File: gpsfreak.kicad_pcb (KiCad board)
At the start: 4 copper layers, 79.8 x 47.2 mm, 177 parts, among them J13 Boot, J2 SMA, J3 SMA, J4 SMA, J5 U.Fl, J6 SMA, J7 USB_C_Receptacle_16P, J8 Conn_01x06, J9 Skedd, SW1 SW_Push, T2 MABA-010247-2R1250, U1 MAX-M10S, U2 LMK05318BRGZR, U3 TG5032CGN, U31 TLV3601DCKR, U4 STM32H503KBUx, U41 TS5A63157DBV, U5 TPSM82822SILR, U6 TPSM82822SILR, U61 TMP117xxDRV, U7 TPS7A8801RTJR, U71 USBLC6-2SC6, U8 LCMXO2-256HC-4SG32C

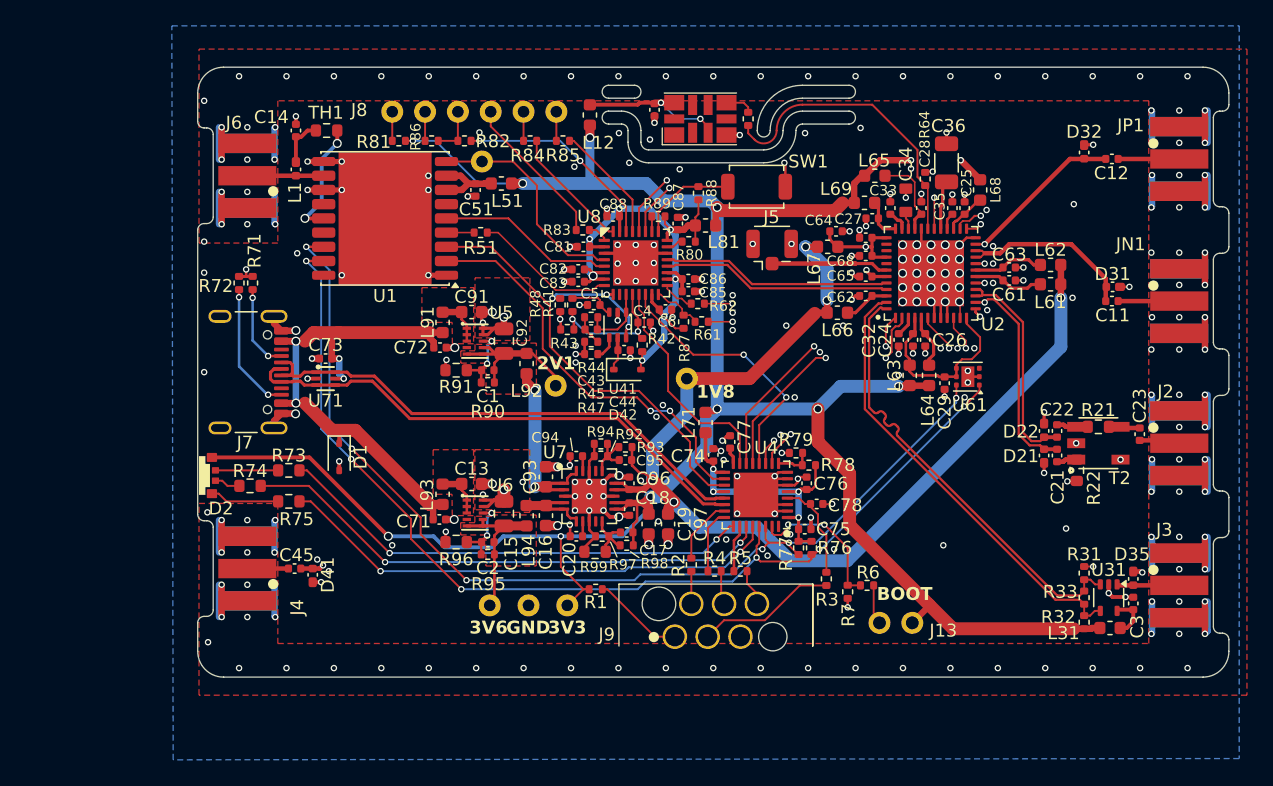
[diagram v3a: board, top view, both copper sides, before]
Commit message: Pull-up on safe-boot.  Juggle things a bit.
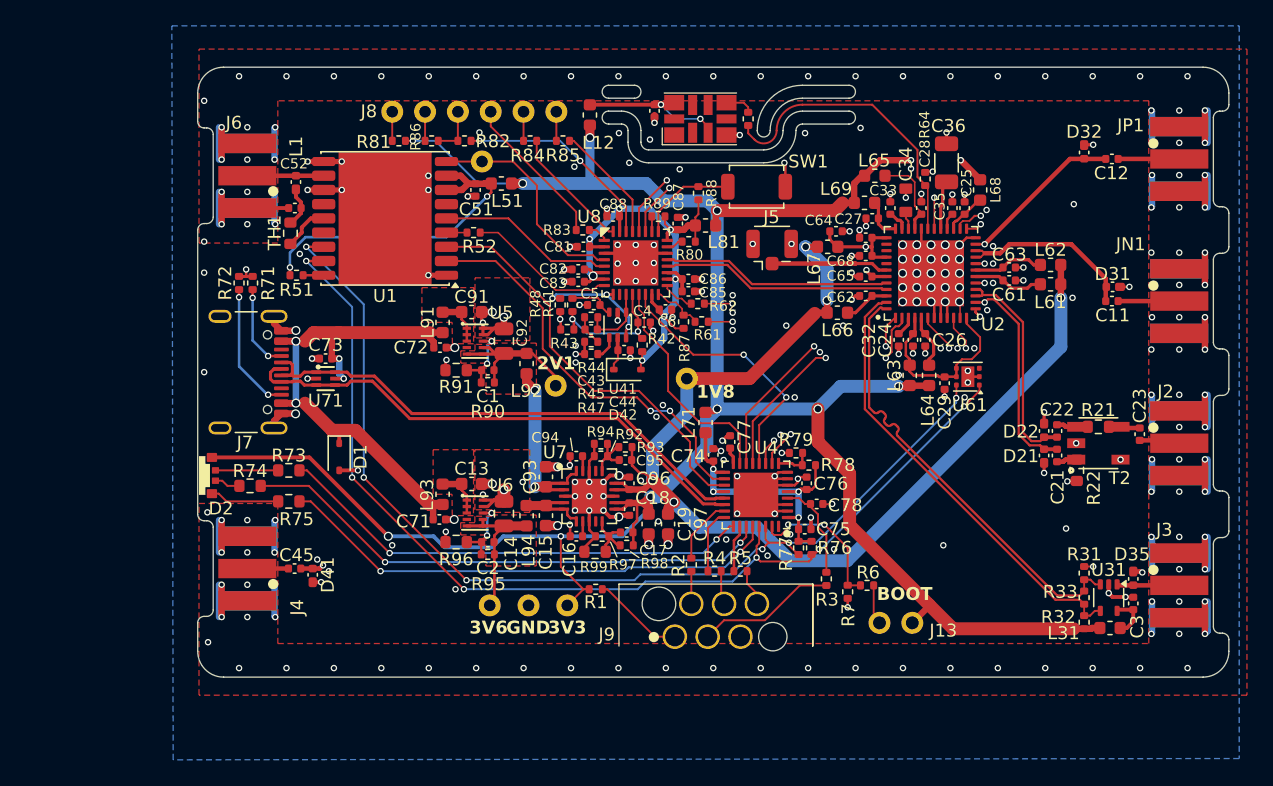
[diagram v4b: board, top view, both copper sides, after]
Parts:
- added R51: 5k1, Resistor_SMD:R_0402_1005Metric, F.Cu at (117.8, 92.5)
- moved TH1 8.43 mm to (117.3, 89.2), turned to -90 degrees
- moved C52 6.00 mm to (117.6, 87.3), turned to 180 degrees
- moved L1 0.97 mm to (117.7, 85.3), turned to -90 degrees
- moved R52 0.55 mm to (131.4, 89.2)
- moved C31 0.08 mm to (145.4, 79.8)
- renumbered C15 to C14, C16 to C15, C20 to C16, C14 to C52, R51 to R52
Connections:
- U1 pad 18: unconnected-(U1-~{SAFEBOOT}-Pad18) -> Net-(U1-~{SAFEBOOT})
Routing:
- net /GPS/VGPS: track 5.63 -> 25.6 mm, vias 0 -> 2
- net /GPS/VCC_RF: track 9.29 -> 3.63 mm, vias 2 -> 0
- net GND: track 206.9 -> 210.2 mm, vias 307 -> 306
- net Net-(U1-~{SAFEBOOT}): track 0.00 -> 1.59 mm
- net Net-(C52-Pad1): track 3.71 -> 3.13 mm
- net Net-(U1-TIMEPULSE): track 2.14 -> 1.59 mm
- net GPSCLK: track 11.0 -> 11.6 mm

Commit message: Tidy up.
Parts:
- added R11: 5k1, Resistor_SMD:R_0402_1005Metric, F.Cu at (146.8, 86.3)
- D42: value 1N5819WS -> RB751S-40; footprint Diode_SMD:D_SOD-323 -> Diode_SMD:D_SOD-523
- U8: value LCMXO2-256HC-4SG32C -> LCMXO2-640HC-4SG48C; footprint Parts:QFN-32-1EP_5x5mm_P0.5mm_EP3.5x3.5mm -> Parts:QFN-48-1EP_7x7mm_P0.5mm_EP5.45x5.45mm
- moved TP4 7.64 mm to (135.6, 93.8)
- moved R42 6.19 mm to (138.3, 97.2), turned to -90 degrees
- moved R87 3.56 mm to (146.2, 99.3), turned to 0 degrees
- moved C83 2.66 mm to (139.3, 95.7)
- moved R41 2.41 mm to (139.3, 97.2)
- moved C85 2.36 mm to (148.2, 96.1), turned to -90 degrees
- moved R45 2.31 mm to (140.8, 100.0), turned to 90 degrees
- moved C87 2.09 mm to (145.8, 87.0)
- moved C84 2.03 mm to (145.8, 97.1), turned to -90 degrees
- moved R43 2.01 mm to (139.2, 98.7)
- moved C43 1.92 mm to (141.1, 98.5)
- moved R44 1.92 mm to (141.1, 97.6)
- moved C42 1.87 mm to (141.1, 96.7)
- moved R61 1.80 mm to (149.1, 94.3)
- moved R47 1.77 mm to (141.7, 100.0), turned to 90 degrees
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- renumbered C4 to C41, C5 to C42, C6 to C84
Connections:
- R61 pad 1: Net-(U8-PB9A) -> Net-(U8-R7D)
- R62 pad 1: Net-(U8-PB9B) -> Net-(U8-R7B)
- R80 pad 2: Net-(U8-PT9D) -> Net-(U8-T11D)
- R87 pad 2: Net-(U8-PB9A) -> GPS_nRSTF
- R89 pad 2: Net-(U8-PT9A) -> Net-(U8-T10C)
- U8 pad 1: /FPGA/TDO -> /FPGA/VFPGA
- U8 pad 11: /FPGA/ClkIO+ -> /FPGA/ClkOEN
- U8 pad 12: /FPGA/ClkIO- -> unconnected-(U8-L6B-Pad12)
- U8 pad 13: GPS_nRSTF -> /FPGA/VFPGA
- U8 pad 14: EXTINTF -> unconnected-(U8-B4A-Pad14)
- U8 pad 15: /FPGA/VFPGA -> unconnected-(U8-B4B-Pad15)
- U8 pad 16: Net-(U8-PB9A) -> unconnected-(U8-B6A-Pad16)
- U8 pad 17: Net-(U8-PB9B) -> unconnected-(U8-B6B-Pad17)
- U8 pad 18: /FPGA/VFPGA -> /FPGA/ClkIO+
- U8 pad 19: /FPGA/VFPGA -> /FPGA/ClkIO-
- U8 pad 2: /FPGA/VFPGA -> unconnected-(U8-L2A-Pad2)
- U8 pad 20: /OUT4_P -> unconnected-(U8-B10C-Pad20)
- U8 pad 21: /OUT4_N -> unconnected-(U8-B10D-Pad21)
- U8 pad 22: GND -> /FPGA/VFPGA
- U8 pad 23: Net-(U8-PT9D) -> GPS_nRSTF
- U8 pad 24: /FPGA/VFPGA -> EXTINTF
- U8 pad 25: /FPGA/PROGN -> /FPGA/VFPGA
- U8 pad 26: Net-(U8-PT9A) -> Net-(U8-R7D)
- U8 pad 27: I2C_SDA -> unconnected-(U8-R7C-Pad27)
- U8 pad 28: I2C_SCL -> Net-(U8-R7B)
- U8 pad 29: /FPGA/TMS -> unconnected-(U8-R7A-Pad29)
- U8 pad 3: GND -> GPS_nRST
- U8 pad 30: /FPGA/TCK -> /FPGA/VFPGA
- U8 pad 31: /FPGA/VFPGA -> unconnected-(U8-R6D-Pad31)
- U8 pad 32: /FPGA/TDI -> unconnected-(U8-R6C-Pad32)
- U8 pad 33: GND -> /OUT4_P
- U8 pad 4: GPS_nRST -> EXTINT
- U8 pad 5: EXTINT -> unconnected-(U8-L2D-Pad5)
- U8 pad 7: /FPGA/VFPGA -> unconnected-(U8-L3A-Pad7)
- U8 pad 8: GPSCLK -> unconnected-(U8-L3B-Pad8)
- U8 pad 9: /FPGA/ClkOEN -> GPSCLK
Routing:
- net /FPGA/VFPGA: track 46.1 -> 54.2 mm, vias 7 -> 10
- net GND: track 210.2 -> 202.5 mm, vias 306 -> 304
- net Net-(U8-PB9A): track 4.01 -> 0.00 mm
- net EXTINTF: track 20.7 -> 18.1 mm
- net Net-(U8-PB9B): track 2.57 -> 0.00 mm
- net /FPGA/PROGN: track 7.70 -> 9.94 mm
- net GPS_nRSTF: track 17.6 -> 15.4 mm
- net Net-(U8-T11C): track 0.00 -> 2.10 mm
- net I2C_SDA: track 127.0 -> 129.1 mm
- net I2C_SCL: track 131.8 -> 133.7 mm
- net GPS2CPU: track 30.8 -> 32.6 mm
- net /FPGA/ClkOEN: track 9.55 -> 7.88 mm, vias 3 -> 2
- net CPU2GPS: track 31.4 -> 33.0 mm
- net Net-(U8-T11D): track 0.00 -> 1.50 mm
- net +1V8: track 85.3 -> 83.8 mm
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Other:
- board text added: "VGCOIM"

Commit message: Back to tps82084...
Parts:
- removed C1, C2: 470p, Capacitor_SMD:C_0402_1005Metric
- R90: value 75k -> 39k
- R91: value 30k -> 24k; footprint Resistor_SMD:R_0603_1608Metric -> Resistor_SMD:R_0402_1005Metric
- R95: value 150k -> 200k
- R96: value 30k -> 46k; footprint Resistor_SMD:R_0603_1608Metric -> Resistor_SMD:R_0402_1005Metric
- U5, U6: value TPSM82822SILR -> TPS82084SIL; footprint Parts:SIL0010D-MFG -> Parts:SIL0008C_SMD_NV
- moved TP5 10.7 mm to (134.2, 107.5)
- moved R90 5.97 mm to (131.7, 94.9), turned to 90 degrees
- moved R95 5.97 mm to (131.7, 108.2), turned to 90 degrees
- moved R96 4.98 mm to (130.7, 108.2), turned to -90 degrees
- moved R91 4.98 mm to (130.7, 94.9), turned to -90 degrees
- moved C13 4.75 mm to (131.2, 113.4)
- moved C91 4.75 mm to (131.2, 100.1)
- moved TP3 3.00 mm to (138.7, 118.0)
- moved TP7 3.00 mm to (135.7, 118.0)
- moved L92 1.75 mm to (135.6, 97.6)
- moved L93 1.48 mm to (128.8, 110.9), turned to -90 degrees
- moved L91 1.48 mm to (128.8, 97.6), turned to -90 degrees
- moved C72 1.30 mm to (127.5, 98.2), turned to 90 degrees
- moved C71 1.25 mm to (127.5, 111.5), turned to 90 degrees
- moved L94 1.16 mm to (135.6, 110.0), turned to -90 degrees
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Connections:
- U5 pad 2: /Power/In2V1 -> unconnected-(U5-PG-Pad2)
- U5 pad 4: unconnected-(U5-PG-Pad4) -> /Power/In2V1
- U5 pad 5: /Power/2V1 -> GND
- U5 pad 6: /Power/2V1 -> GND
- U5 pad 7: /Power/2V1 -> /Power/Fb21
- U5 pad 8: /Power/Fb21 -> /Power/2V1
- U6 pad 2: /Power/In3V6 -> unconnected-(U6-PG-Pad2)
- U6 pad 4: unconnected-(U6-PG-Pad4) -> /Power/In3V6
- U6 pad 5: /Power/3V6 -> GND
- U6 pad 6: /Power/3V6 -> GND
- U6 pad 7: /Power/3V6 -> /Power/Fb36
- U6 pad 8: /Power/Fb36 -> /Power/3V6
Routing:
- net GND: track 202.5 -> 212.2 mm
- net /Power/2V1: track 13.5 -> 7.59 mm
- net /Power/3V6: track 11.2 -> 8.20 mm
- net /Power/In2V1: track 3.88 -> 6.36 mm
- net /Power/In3V6: track 3.88 -> 6.23 mm
- net VBus: track 43.0 -> 41.5 mm
- net /Power/In1V8: track 13.4 -> 14.6 mm
- net +3V3: track 189.3 -> 190.4 mm, vias 12 -> 11

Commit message: Ordered.
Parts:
- C75, C76: value 0u1 -> 1u
- R96: value 46k -> 56k
- moved TP4 1.46 mm to (134.2, 94.2)
- moved C78 0.40 mm to (157.7, 110.0)
- moved J5 0.20 mm to (155.3, 90.5)
- moved L67 0.20 mm to (159.3, 90.3)
- turned C64 to 180 degrees
- renumbered R47 to R46, R48 to R47, U41 to U9
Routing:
- net GND: track 212.2 -> 211.9 mm, vias 304 -> 303

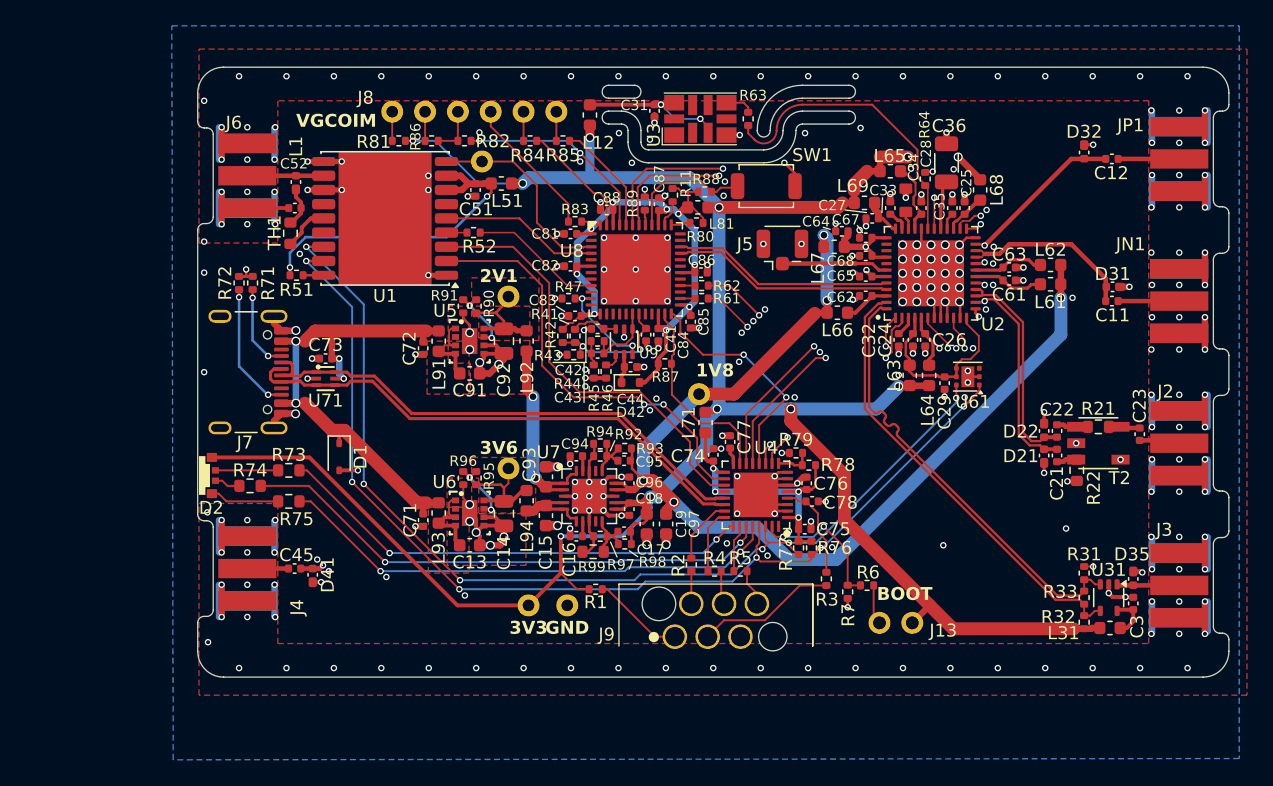
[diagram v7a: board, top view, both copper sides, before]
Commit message: Adjustments.  Silk screen clearance.
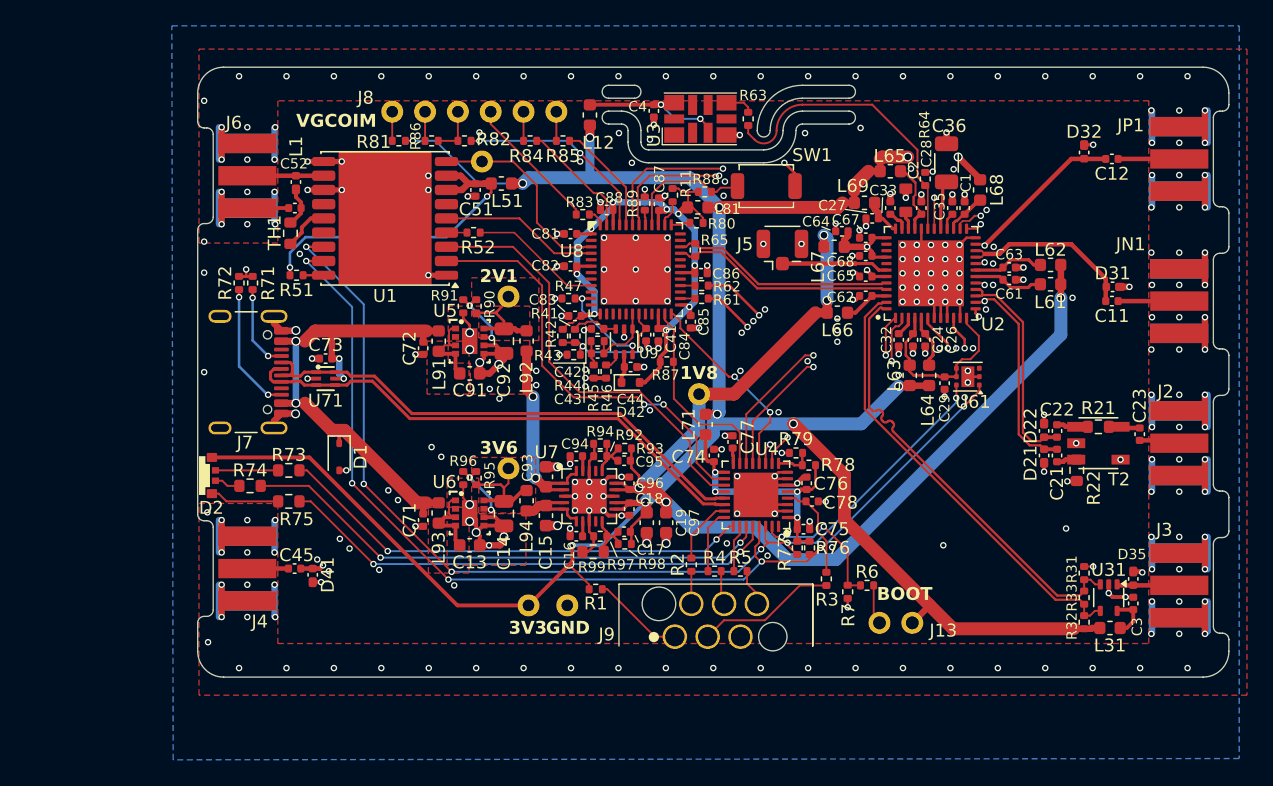
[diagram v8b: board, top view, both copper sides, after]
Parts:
- added R65: 100, Resistor_SMD:R_0402_1005Metric, F.Cu at (148.6, 90.5)
- moved R83 0.81 mm to (139.9, 87.8)
- moved R87 0.21 mm to (146.4, 99.2)
- moved C77 0.20 mm to (151.5, 105.4)
- moved R76 0.15 mm to (157.4, 113.6)
- moved L71 0.15 mm to (149.4, 104.0)
- moved C75 0.10 mm to (157.0, 112.2)
- moved C19 0.10 mm to (144.8, 111.7)
- moved C97 0.10 mm to (146.3, 111.7)
- moved R77 0.10 mm to (156.5, 113.6)
- moved C74 0.07 mm to (150.1, 106.5)
- moved C61 0.05 mm to (172.9, 92.8)
- renumbered C25 to C1, C34 to C2, C31 to C4
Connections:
- net /Output2/Ext2 renamed /Output2/Ext
- net /Output3/Ext3 renamed /Output3/Ext
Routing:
- net +3V3: track 190.7 -> 187.0 mm
- net GND: track 211.9 -> 209.2 mm, vias 303 -> 316
- net EXTINTF: track 18.1 -> 15.5 mm
- net /CPU/VCPU: track 22.9 -> 22.2 mm
